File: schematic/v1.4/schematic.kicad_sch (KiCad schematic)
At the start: 16 parts, among them J1 USB_C_Receptacle_USB2.0_16P, J2 Connector, Q1 AO3401, Q2 2N2222, U1 ESP32-C3, U2 MAX4466, U5 WS2812B, U6 AMS1117

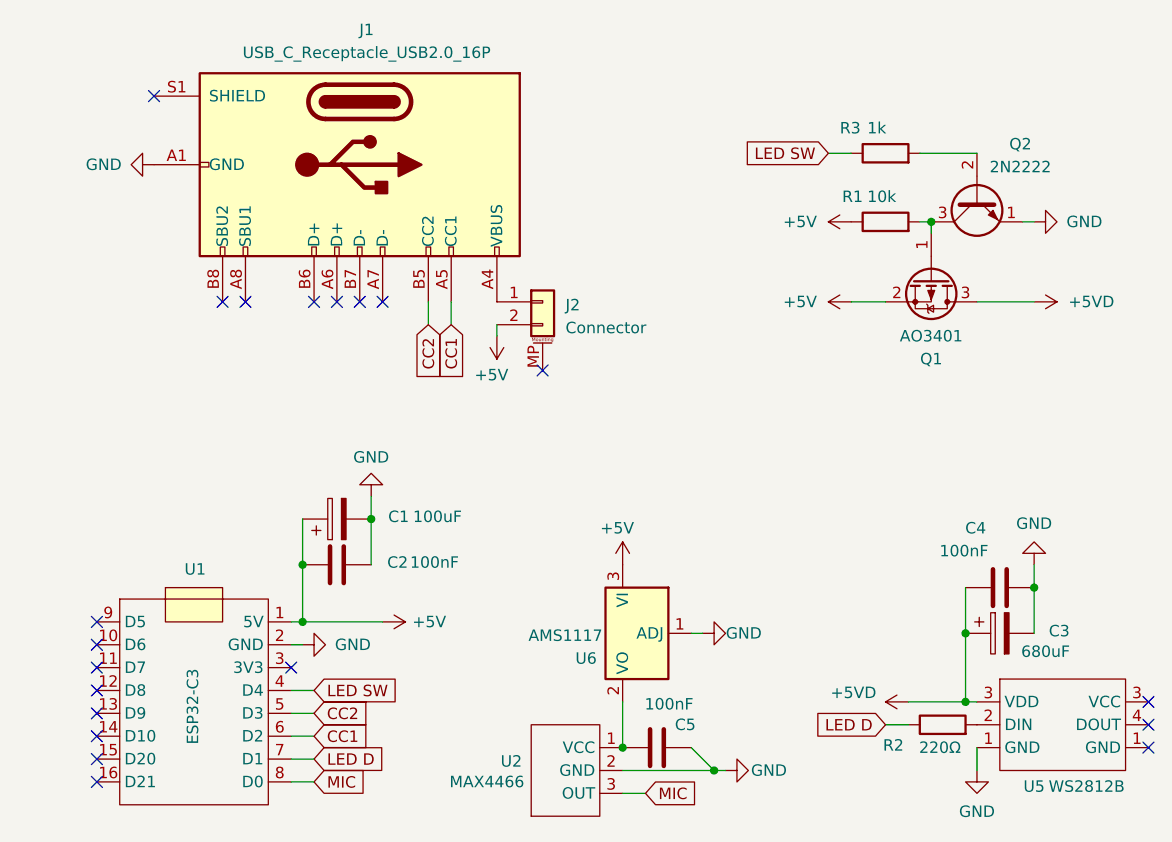
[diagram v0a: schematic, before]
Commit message: Add support for usb c and a power communication with cutoff
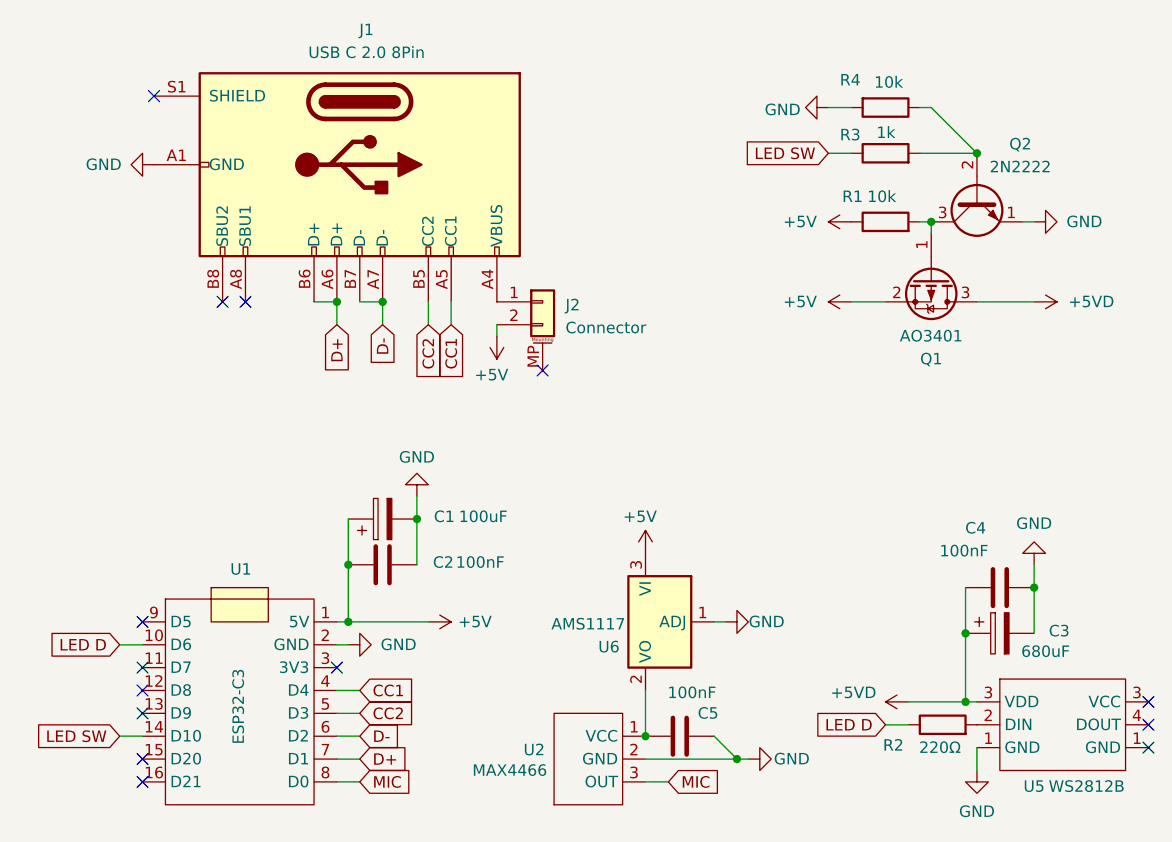
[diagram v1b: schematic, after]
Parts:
- added R4: 10k, Resistor_THT:R_Axial_DIN0207_L6.3mm_D2.5mm_P7.62mm_Horizontal, symbol Device:R
- J1: value USB_C_Receptacle_USB2.0_16P -> USB C 2.0 8Pin
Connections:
- net CC1: now also U1.4 (D4); no longer U1.6 (D2)
- net GND: now also R4.2
- net LED D: now also U1.10 (D6); no longer U1.7 (D1)
- net LED SW: now also U1.14 (D10); no longer U1.4 (D4)
- net D+: now reaches J1.A6 (D+)
- net D+: now also J1.B6 (D+), U1.7 (D1)
- net D-: now reaches J1.A7 (D-)
- net D-: now also J1.B7 (D-), U1.6 (D2)
- net at Q2.2 (B), R3.2: now also R4.1
- no-connect marks 20 -> 14
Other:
- moved on the sheet: C1, C2, C5, U1, U2, U6

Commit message: Add usb a power support
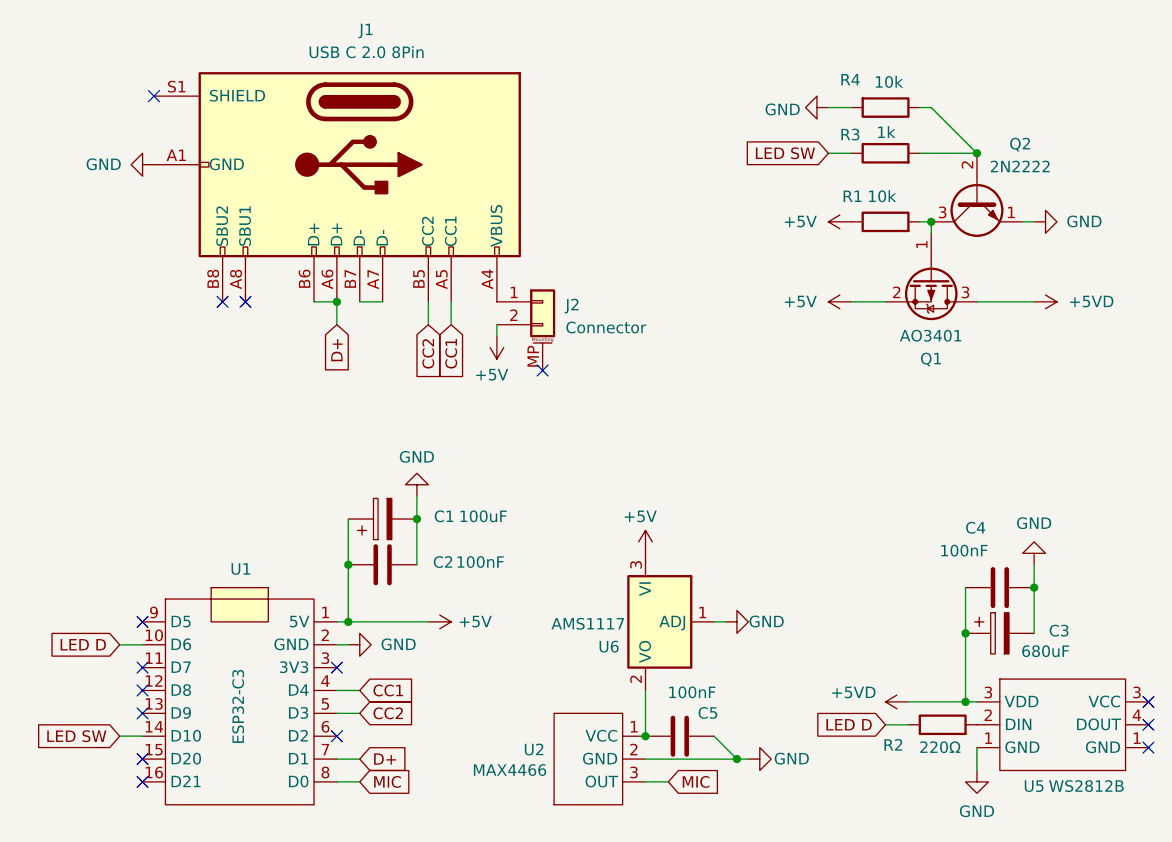
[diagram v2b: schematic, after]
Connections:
- net D-: no longer names the net of J1.A7 (D-), J1.B7 (D-)
- net D-: no longer U1.6 (D2)
- no-connect marks 14 -> 15
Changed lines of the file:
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@@
-	)
-	(junction
-		(at 50.8 44.45)
-		(diameter 0)
-		(color 0 0 0 0)
 	)
 	(junction
@@
 	)
 	(no_connect
+		(at 45.72 92.71)
+	)
+	(no_connect
 		(at 24.13 95.25)
 	)
@@
 	(wire
 		(pts
-			(xy 45.72 92.71) (xy 48.26 92.71)
-		)
-		(stroke
-			(width 0)
-			(type default)
-		)
-	)
-	(wire
-		(pts
 			(xy 102.87 44.45) (xy 106.68 44.45)
 		)
@@
 	(wire
 		(pts
-			(xy 50.8 44.45) (xy 50.8 46.99)
-		)
-		(stroke
-			(width 0)
-			(type default)
-		)
-	)
-	(wire
-		(pts
 			(xy 111.76 22.86) (xy 116.84 27.94)
 		)
@@
 		)
 	)
-	(global_label "D-"
-		(shape input)
-		(at 48.26 92.71 0)
+	(global_label "CC1"
+		(shape input)
+		(at 58.42 46.99 270)
+		(fields_autoplaced yes)
+		(effects
+			(font
+				(size 1.27 1.27)
+			)
+			(justify right)
+		)
+		(property "Intersheetrefs" "${INTERSHEET_REFS}"
+			(at 58.42 52.9502 90)
+			(effects
+				(font
+					(size 1.27 1.27)
+				)
+				(justify right)
+				(hide yes)
+			)
+		)
+	)
+	(global_label "LED SW"
+		(shape input)
+		(at 100.33 27.94 180)
+		(fields_autoplaced yes)
+		(effects
+			(font
+				(size 1.27 1.27)
+			)
+			(justify right)
+		)
+		(property "Intersheetrefs" "${INTERSHEET_REFS}"
+			(at 91.1724 27.94 0)
+			(effects
+				(font
+					(size 1.27 1.27)
+				)
+				(justify right)
+				(hide yes)
+			)
+		)
+	)
+	(global_label "D+"
+		(shape input)
+		(at 45.72 46.99 270)
+		(fields_autoplaced yes)
+		(effects
+			(font
+				(size 1.27 1.27)
+			)
+			(justify right)
+		)
+		(property "Intersheetrefs" "${INTERSHEET_REFS}"
+			(at 45.72 51.8844 90)
+			(effects
+				(font
+					(size 1.27 1.27)
+				)
+				(justify right)
+				(hide yes)
+			)
+		)
+	)
+	(global_label "CC2"
+		(shape input)
+		(at 55.88 46.99 270)
+		(fields_autoplaced yes)
+		(effects
+			(font
+				(size 1.27 1.27)
+			)
+			(justify right)
+		)
+		(property "Intersheetrefs" "${INTERSHEET_REFS}"
+			(at 55.88 52.9502 90)
+			(effects
+				(font
+					(size 1.27 1.27)
+				)
+				(justify right)
+				(hide yes)
+			)
+		)
+	)
+	(global_label "D+"
+		(shape input)
+		(at 48.26 95.25 0)
 		(fields_autoplaced yes)
 		(effects
@@
 		)
 		(property "Intersheetrefs" "${INTERSHEET_REFS}"
-			(at 53.1544 92.71 0)
+			(at 53.1544 95.25 0)
 			(effects
 				(font
@@
 				(hide yes)
 			)
-		)
-	)
-	(global_label "CC1"
-		(shape input)
-		(at 58.42 46.99 270)
-		(fields_autoplaced yes)
-		(effects
-			(font
-				(size 1.27 1.27)
-			)
-			(justify right)
-		)
-		(property "Intersheetrefs" "${INTERSHEET_REFS}"
-			(at 58.42 52.9502 90)
-			(effects
-				(font
-					(size 1.27 1.27)
-				)
-				(justify right)
-				(hide yes)
-			)
-		)
-	)
-	(global_label "LED SW"
-		(shape input)
-		(at 100.33 27.94 180)
-		(fields_autoplaced yes)
-		(effects
-			(font
-				(size 1.27 1.27)
-			)
-			(justify right)
-		)
-		(property "Intersheetrefs" "${INTERSHEET_REFS}"
-			(at 91.1724 27.94 0)
-			(effects
-				(font
-					(size 1.27 1.27)
-				)
-				(justify right)
-				(hide yes)
-			)
-		)
-	)
-	(global_label "D+"
-		(shape input)
-		(at 45.72 46.99 270)
-		(fields_autoplaced yes)
-		(effects
-			(font
-				(size 1.27 1.27)
-			)
-			(justify right)
-		)
-		(property "Intersheetrefs" "${INTERSHEET_REFS}"
-			(at 45.72 51.8844 90)
-			(effects
-				(font
-					(size 1.27 1.27)
-				)
-				(justify right)
-				(hide yes)
-			)
-		)
-	)
-	(global_label "CC2"
-		(shape input)
-		(at 55.88 46.99 270)
-		(fields_autoplaced yes)
-		(effects
-			(font
-				(size 1.27 1.27)
-			)
-			(justify right)
-		)
-		(property "Intersheetrefs" "${INTERSHEET_REFS}"
-			(at 55.88 52.9502 90)
-			(effects
-				(font
-					(size 1.27 1.27)
-				)
-				(justify right)
-				(hide yes)
-			)
-		)
-	)
-	(global_label "D+"
-		(shape input)
-		(at 48.26 95.25 0)
-		(fields_autoplaced yes)
-		(effects
-			(font
-				(size 1.27 1.27)
-			)
-			(justify left)
-		)
-		(property "Intersheetrefs" "${INTERSHEET_REFS}"
-			(at 53.1544 95.25 0)
-			(effects
-				(font
-					(size 1.27 1.27)
-				)
-				(justify left)
-				(hide yes)
-			)
-		)
-	)
-	(global_label "D-"
-		(shape input)
-		(at 50.8 46.99 270)
-		(fields_autoplaced yes)
-		(effects
-			(font
-				(size 1.27 1.27)
-			)
-			(justify right)
-		)
-		(property "Intersheetrefs" "${INTERSHEET_REFS}"
-			(at 50.8 51.8844 90)
-			(effects
-				(font
-					(size 1.27 1.27)
-				)
-				(justify right)
-				(hide yes)
-			)

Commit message: Add D+ pull up
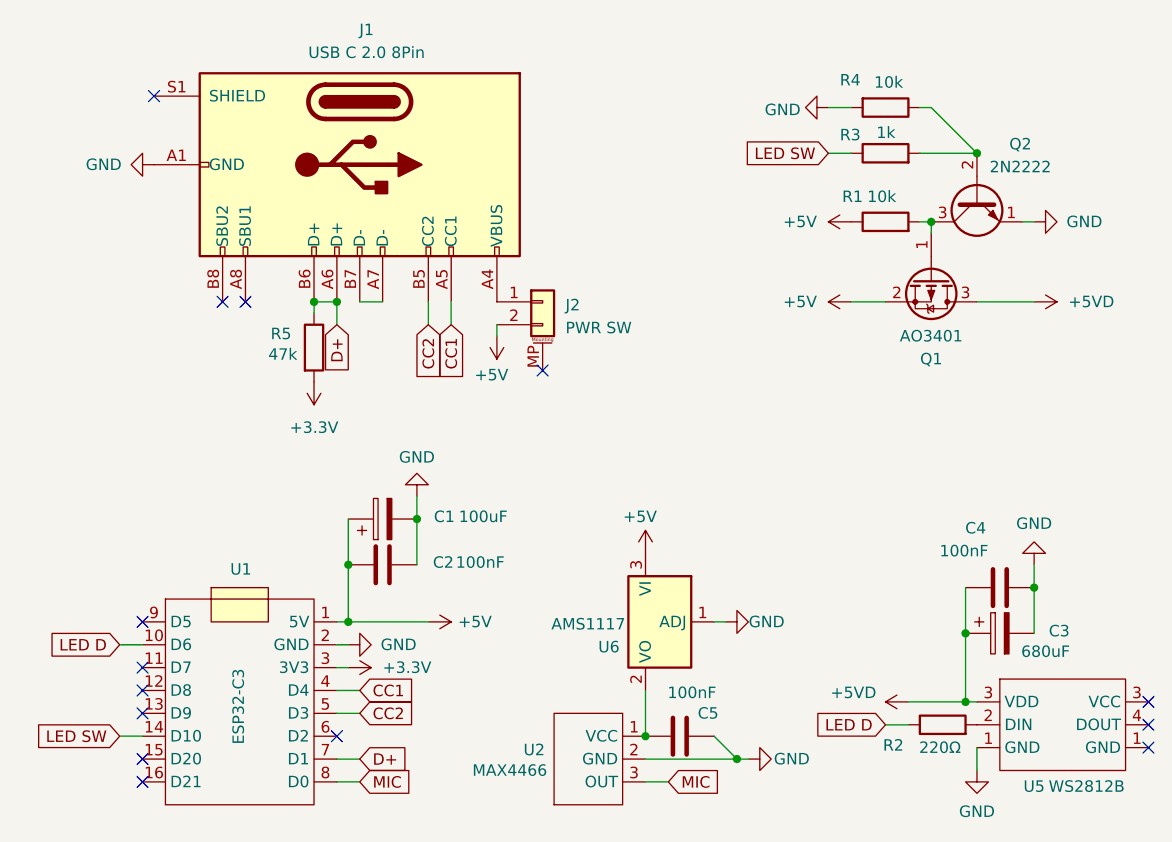
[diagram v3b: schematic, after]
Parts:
- added R5: 47k, Resistor_THT:R_Axial_DIN0207_L6.3mm_D2.5mm_P7.62mm_Horizontal, symbol Device:R
- J2: value Connector -> PWR SW
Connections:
- net D+: now also R5.1
- net +3.3V: now reaches U1.3 (3V3)
- net +3.3V: now also R5.2
- no-connect marks 15 -> 14
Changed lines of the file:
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@@
+	)
+	(junction
+		(at 43.18 44.45)
+		(diameter 0)
+		(color 0 0 0 0)
 	)
 	(junction
@@
 	)
 	(no_connect
-		(at 45.72 85.09)
-	)
-	(no_connect
 		(at 25.4 21.59)
 	)
@@
 		(pts
 			(xy 45.72 97.79) (xy 48.26 97.79)
+		)
+		(stroke
+			(width 0)
+			(type default)
+		)
+	)
+	(wire
+		(pts
+			(xy 45.72 85.09) (xy 46.99 85.09)
+		)
+		(stroke
+			(width 0)
+			(type default)
+		)
+	)
+	(wire
+		(pts
+			(xy 43.18 44.45) (xy 43.18 45.72)
 		)
 		(stroke
@@
 	)
 	(symbol
+		(lib_id "Device:R")
+		(at 43.18 49.53 0)
+		(unit 1)
+		(exclude_from_sim no)
+		(in_bom yes)
+		(on_board yes)
+		(dnp no)
+		(property "Reference" "R5"
+			(at 38.354 48.006 0)
+			(effects
+				(font
+					(size 1.27 1.27)
+				)
+				(justify left)
+			)
+		)
+		(property "Value" "47k"
+			(at 38.1 50.292 0)
+			(effects
+				(font
+					(size 1.27 1.27)
+				)
+				(justify left)
+			)
+		)
+		(property "Footprint" "Resistor_THT:R_Axial_DIN0207_L6.3mm_D2.5mm_P7.62mm_Horizontal"
+			(at 41.402 49.53 90)
+			(effects
+				(font
+					(size 1.27 1.27)
+				)
+				(hide yes)
+			)
+		)
+		(property "Datasheet" "~"
+			(at 43.18 49.53 0)
+			(effects
+				(font
+					(size 1.27 1.27)
+				)
+				(hide yes)
+			)
+		)
+		(property "Description" "Resistor"
+			(at 43.18 49.53 0)
+			(effects
+				(font
+					(size 1.27 1.27)
+				)
+				(hide yes)
+			)
+		)
+		(pin "2"
+		)
+		(pin "1"
+		)
+		(instances
+			(project "schematic"
+				(path "/1685a75f-db20-476f-a7be-a6eea2d7b7b5"
+					(reference "R5")
+					(unit 1)
+				)
+			)
+		)
+	)
+	(symbol
+		(lib_id "power:+3.3V")
+		(at 46.99 85.09 270)
+		(unit 1)
+		(exclude_from_sim no)
+		(in_bom yes)
+		(on_board yes)
+		(dnp no)
+		(fields_autoplaced yes)
+		(property "Reference" "#PWR017"
+			(at 43.18 85.09 0)
+			(effects
+				(font
+					(size 1.27 1.27)
+				)
+				(hide yes)
+			)
+		)
+		(property "Value" "+3.3V"
+			(at 50.8 85.0899 90)
+			(effects
+				(font
+					(size 1.27 1.27)
+				)
+				(justify left)
+			)
+		)
+		(property "Footprint" ""
+			(at 46.99 85.09 0)
+			(effects
+				(font
+					(size 1.27 1.27)
+				)
+				(hide yes)
+			)
+		)
+		(property "Datasheet" ""
+			(at 46.99 85.09 0)
+			(effects
+				(font
+					(size 1.27 1.27)
+				)
+				(hide yes)
+			)
+		)
+		(property "Description" "Power symbol creates a global label with name \"+3.3V\""
+			(at 46.99 85.09 0)
+			(effects
+				(font
+					(size 1.27 1.27)
+				)
+				(hide yes)
+			)
+		)
+		(pin "1"
+		)
+		(instances
+			(project "schematic"
+				(path "/1685a75f-db20-476f-a7be-a6eea2d7b7b5"
+					(reference "#PWR017")
+					(unit 1)
+				)
+			)
+		)
+	)
+	(symbol
 		(lib_id "power:GND")
 		(at 116.84 96.52 0)
@@
 	)
 	(symbol
+		(lib_id "power:+3.3V")
+		(at 43.18 53.34 180)
+		(unit 1)
+		(exclude_from_sim no)
+		(in_bom yes)
+		(on_board yes)
+		(dnp no)
+		(fields_autoplaced yes)
+		(property "Reference" "#PWR014"
+			(at 43.18 49.53 0)
+			(effects
+				(font
+					(size 1.27 1.27)
+				)
+				(hide yes)
+			)
+		)
+		(property "Value" "+3.3V"
+			(at 43.18 58.42 0)
+			(effects
+				(font
+					(size 1.27 1.27)
+				)
+			)
+		)
+		(property "Footprint" ""
+			(at 43.18 53.34 0)
+			(effects
+				(font
+					(size 1.27 1.27)
+				)
+				(hide yes)
+			)
+		)
+		(property "Datasheet" ""
+			(at 43.18 53.34 0)
+			(effects
+				(font
+					(size 1.27 1.27)
+				)
+				(hide yes)
+			)
+		)
+		(property "Description" "Power symbol creates a global label with name \"+3.3V\""
+			(at 43.18 53.34 0)
+			(effects
+				(font
+					(size 1.27 1.27)
+				)
+				(hide yes)
+			)
+		)
+		(pin "1"
+		)
+		(instances
+			(project ""
+				(path "/1685a75f-db20-476f-a7be-a6eea2d7b7b5"
+					(reference "#PWR014")
+					(unit 1)
+				)
+			)
+		)
+	)
+	(symbol
 		(lib_id "power:+5VA")
 		(at 55.88 80.01 270)
@@
 			)
 		)
-		(property "Value" "Connector"
+		(property "Value" "PWR SW"
 			(at 71.12 47.3455 0)
 			(effects

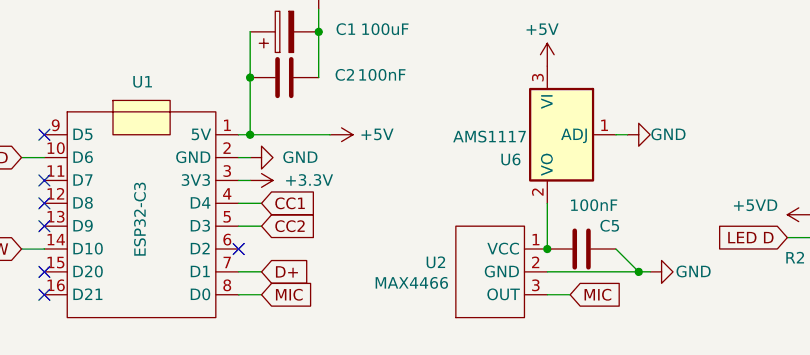
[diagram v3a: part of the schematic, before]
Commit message: Adjust pcb and add icons to webserver
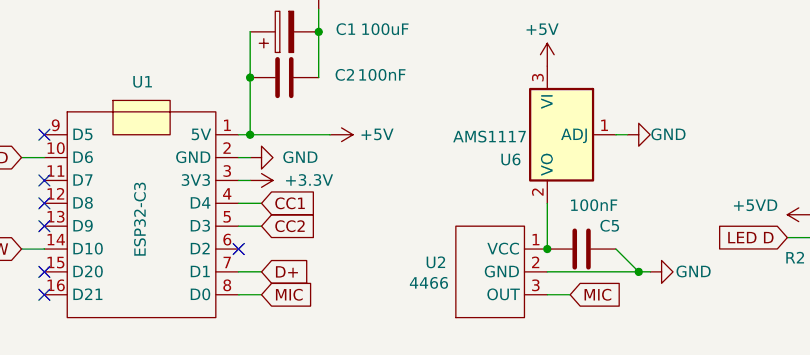
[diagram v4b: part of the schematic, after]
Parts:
- U2: value MAX4466 -> 4466
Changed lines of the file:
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@@
 			)
 		)
-		(property "Value" "MAX4466"
+		(property "Value" "4466"
 			(at 69.088 96.52 90)
 			(effects

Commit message: Final tweaks to pcb
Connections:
- net at J1.A7 (D-): no longer J1.B7 (D-)
- no-connect marks 14 -> 16
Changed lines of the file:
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@@
+	)
+	(no_connect
+		(at 50.8 44.45)
 	)
 	(no_connect
@@
 	)
 	(no_connect
+		(at 48.26 44.45)
+	)
+	(no_connect
 		(at 135.89 88.9)
 	)
@@
 		)
 		(stroke
-			(width 0)
-			(type default)
-		)
-	)
-	(wire
-		(pts
-			(xy 48.26 44.45) (xy 50.8 44.45)
-		)
-		(stroke
